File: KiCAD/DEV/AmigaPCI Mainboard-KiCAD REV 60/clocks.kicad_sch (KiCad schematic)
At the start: 46 parts, among them U108 74AHC04, U210 AT27C4096, U211 AT27C4096, U219 74AHCT04, U230 74LVC157, U812 74LVC245, U813 74LVC245, U814 74LVC245, U815 74LVC08, U816 74LVC245, U817 74LVC245, U818 74LVC245, U819 74LVC245, X1 6MHz, X2 33MHz, X3 28.63636MHz

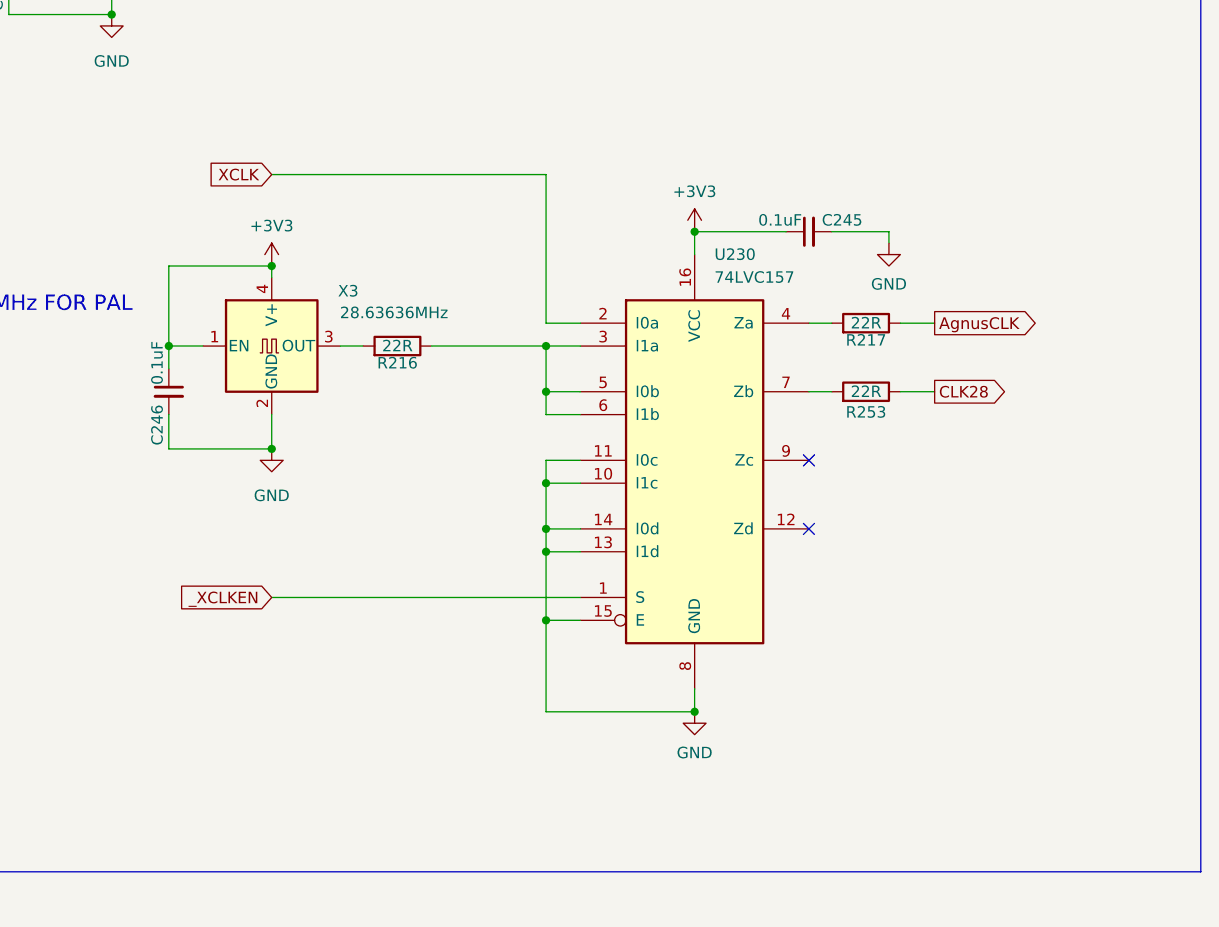
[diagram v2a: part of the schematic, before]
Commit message: APCI Rev 6.0 Work
Eliminate U230 (74LVC147) by moving the clock switching function to U409.
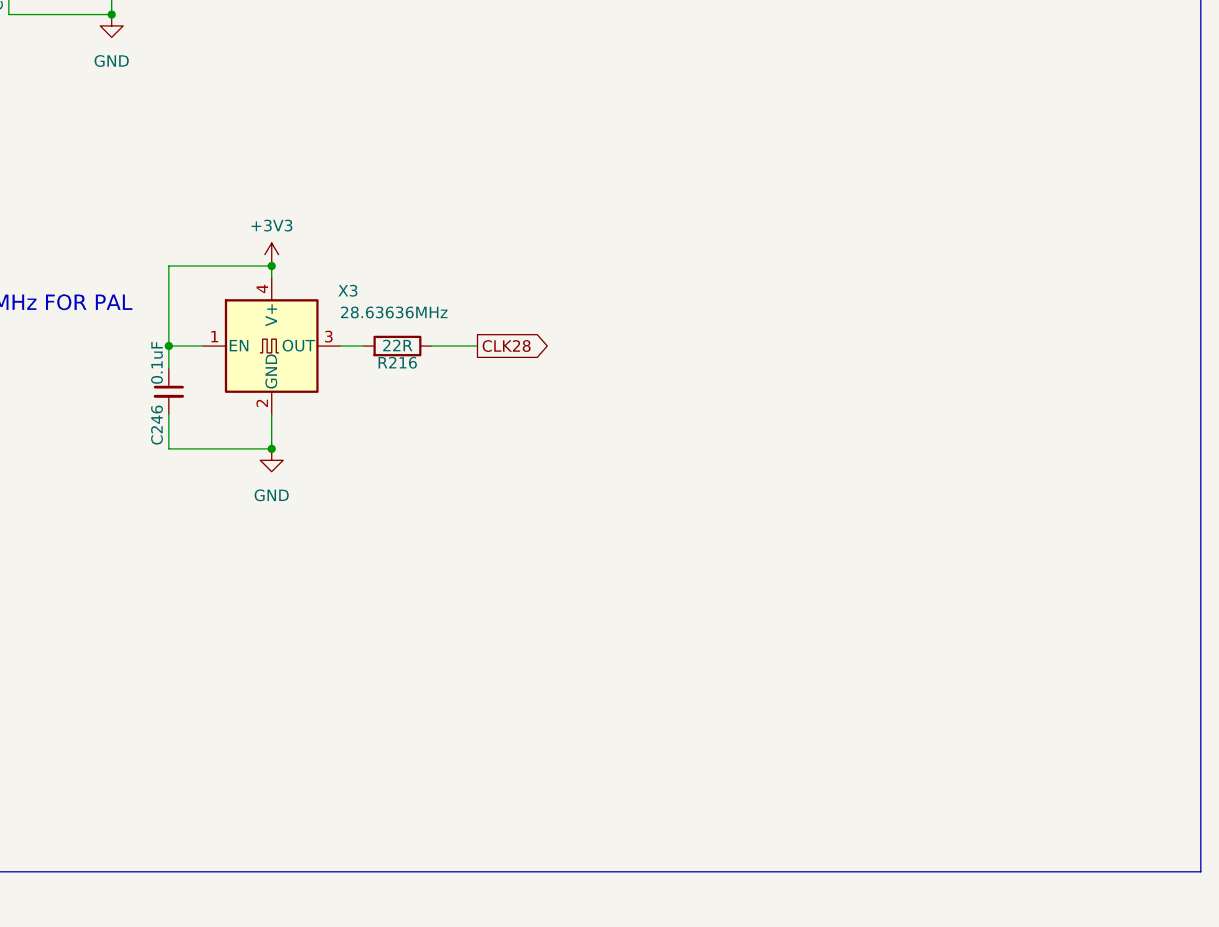
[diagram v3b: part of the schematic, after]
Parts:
- removed C245: 0.1uF, Capacitor_SMD:C_0603_1608Metric, symbol Device:C_Small
- removed R217, R253: 22R, Resistor_SMD:R_0603_1608Metric, symbol Device:R
- removed U230: 74LVC157, Package_SO:TSSOP-16_4.4x5mm_P0.65mm, symbol 74xx:74LS157
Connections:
- net CLK28: now also R216.1
- no-connect marks 2 -> 0

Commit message: Add flash and remove HID buffer.
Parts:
- added C253: 0.1uF, Capacitor_SMD:C_0603_1608Metric, symbol Device:C_Small
- added U223: SST39VF1601C, Package_SO:TSOP-I-48_18.4x12mm_P0.5mm, symbol AmigaPCI-Symbols:SST39VF1601C
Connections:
- net +3V3: now also C253.1, U223.14 (_WP), U223.37 (VDD)
- net GND: now also C253.2, U223.27 (GND), U223.46 (GND)
- new net: U223.10 (NC), U223.13 (NC), U223.47 (NC)
- new net FBANK0: U223.16 (A18)
- new net FBANK1: U223.9 (A19)
- new net FRDY: U223.15 (RY_BY)
- new net LVA1: U223.25 (A0)
- new net LVA10: U223.7 (A9)
- new net LVA11: U223.6 (A10)
- new net LVA12: U223.5 (A11)
- new net LVA13: U223.4 (A12)
- new net LVA14: U223.3 (A13)
- new net LVA15: U223.2 (A14)
- new net LVA16: U223.1 (A15)
- new net LVA17: U223.48 (A16)
- new net LVA18: U223.17 (A17)
- new net LVA2: U223.24 (A1)
- new net LVA3: U223.23 (A2)
- new net LVA4: U223.22 (A3)
- new net LVA5: U223.21 (A4)
- new net LVA6: U223.20 (A5)
- new net LVA7: U223.19 (A6)
- new net LVA8: U223.18 (A7)
- new net LVA9: U223.8 (A8)
- new net LVD16: U223.29 (D0)
- new net LVD17: U223.31 (D1)
- new net LVD18: U223.33 (D2)
- new net LVD19: U223.35 (D3)
- new net LVD20: U223.38 (D4)
- new net LVD21: U223.40 (D5)
- new net LVD22: U223.42 (D6)
- new net LVD23: U223.44 (D7)
- new net LVD24: U223.30 (D8)
- new net LVD25: U223.32 (D9)
- new net LVD26: U223.34 (D10)
- new net LVD27: U223.36 (D11)
- new net LVD28: U223.39 (D12)
- new net LVD29: U223.41 (D13)
- new net LVD30: U223.43 (D14)
- new net LVD31: U223.45 (D15)
- new net _FEN: U223.26 (_CE)
- new net _FRDEN: U223.28 (_OE)
- new net _FRST: U223.12 (_RST)
- new net _FWREN: U223.11 (_WE)
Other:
- note added: "BOTTOM BOOT 1Mx16 FLASH TREATED AS FOUR 512K ADDRESS SPACES AS DEFINED BY FBANKx."
- note added: "FLASH"
- moved on the sheet: C228, C229, C246, C816, C817, C818, C819, R140, R141, R142, R143, R144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

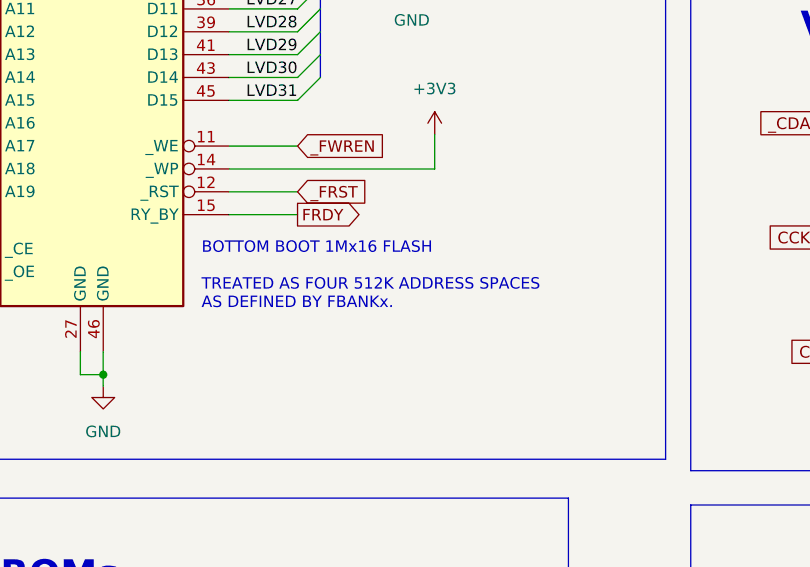
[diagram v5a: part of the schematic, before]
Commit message: APCI Rev 6.0 Work
Added flash and i2c, USB now powered by standbay rail.
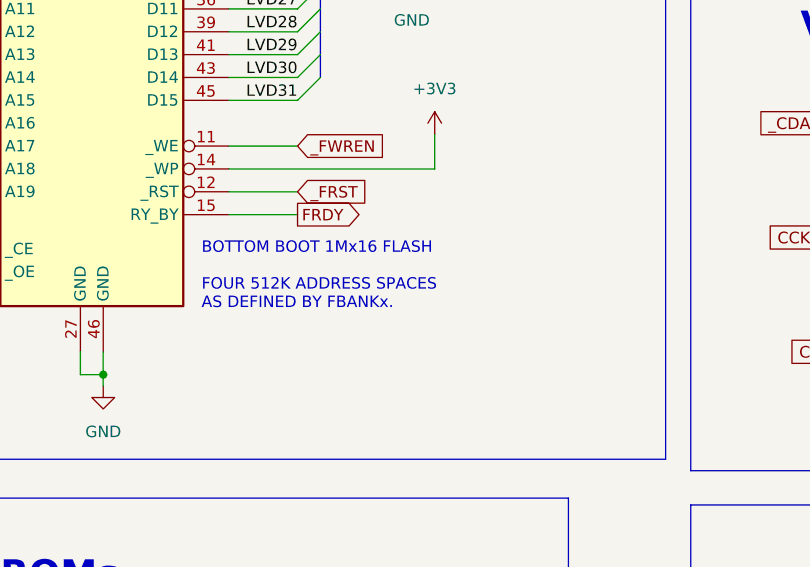
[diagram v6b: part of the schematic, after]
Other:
- note added: "BOTTOM BOOT 1Mx16 FLASH FOUR 512K ADDRESS SPACES AS DEFINED BY FBANKx."
- note removed: "BOTTOM BOOT 1Mx16 FLASH TREATED AS FOUR 512K ADDRESS SPACES AS DEFINED BY FBANKx."
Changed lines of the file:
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@@
 	(title_block
 		(title "AMIGA PCI")
-		(date "2025-06-26")
+		(date "2025-06-27")
 		(rev "6.0")
 	)
@@
 		)
 	)
-	(text "BOTTOM BOOT 1Mx16 FLASH\n\nTREATED AS FOUR 512K ADDRESS SPACES\nAS DEFINED BY FBANKx."
+	(text "BOTTOM BOOT 1Mx16 FLASH\n\nFOUR 512K ADDRESS SPACES\nAS DEFINED BY FBANKx."
 		(exclude_from_sim no)
 		(at 90.932 98.298 0)

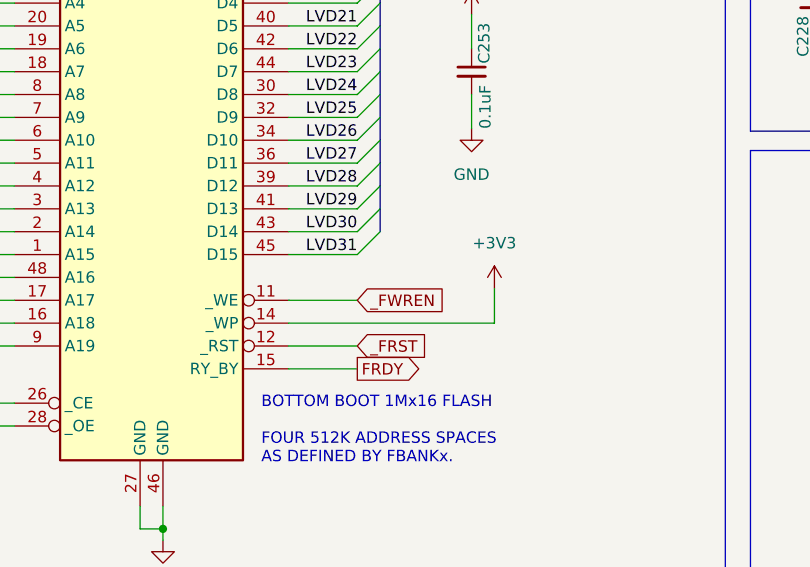
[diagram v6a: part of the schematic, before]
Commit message: APCI Rev 6.0 Work
Add pullups to i2c lines.
Connect Flash _WP to U409.
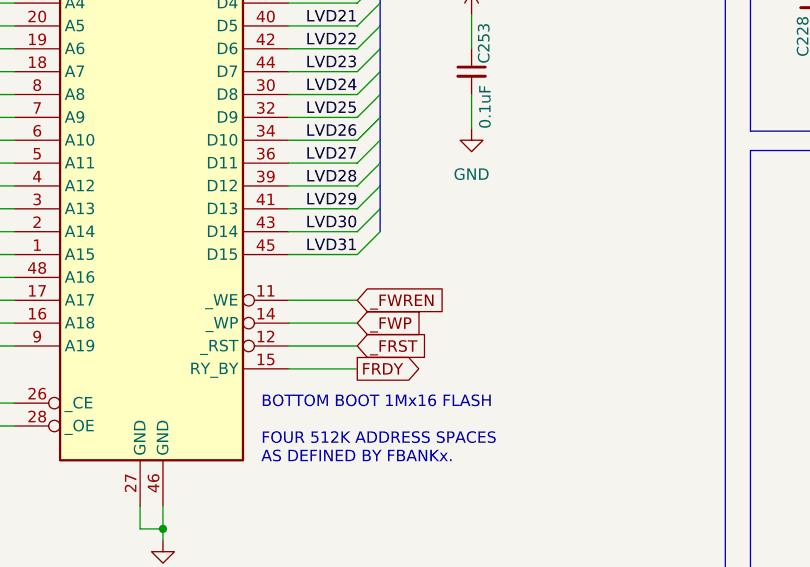
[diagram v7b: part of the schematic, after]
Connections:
- net +3V3: no longer U223.14 (_WP)
- new net _FWP: U223.14 (_WP)
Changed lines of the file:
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@@
 		)
 	)
-	(wire
-		(pts
-			(xy 116.84 82.55) (xy 116.84 86.36)
-		)
-		(stroke
-			(width 0)
-			(type default)
-		)
-	)
 	(bus
 		(pts
@@
 	(wire
 		(pts
+			(xy 101.6 86.36) (xy 93.98 86.36)
+		)
+		(stroke
+			(width 0)
+			(type default)
+		)
+	)
+	(wire
+		(pts
 			(xy 317.5 139.7) (xy 323.85 139.7)
 		)
@@
 	(wire
 		(pts
-			(xy 93.98 86.36) (xy 116.84 86.36)
-		)
-		(stroke
-			(width 0)
-			(type default)
-		)
-	)
-	(wire
-		(pts
 			(xy 325.12 44.45) (xy 317.5 44.45)
 		)
@@
 		)
 	)
+	(global_label "_FWP"
+		(shape input)
+		(at 101.6 86.36 0)
+		(fields_autoplaced yes)
+		(effects
+			(font
+				(size 1.27 1.27)
+			)
+			(justify left)
+		)
+		(property "Intersheetrefs" "${INTERSHEET_REFS}"
+			(at 111.8423 86.36 0)
+			(effects
+				(font
+					(size 1.27 1.27)
+				)
+				(justify left)
+			)
+		)
+	)
 	(global_label "_VC1"
 		(shape output)
@@
 					(unit 1)
 				)
-			)
-		)
-	)
-	(symbol
-		(lib_name "+3V3_1")
-		(lib_id "power:+3V3")
-		(at 116.84 82.55 0)
-		(unit 1)
-		(exclude_from_sim no)
-		(in_bom yes)
-		(on_board yes)
-		(dnp no)
-		(fields_autoplaced yes)
-		(property "Reference" "#PWR149"
-			(at 116.84 86.36 0)
-			(effects
-				(font
-					(size 1.27 1.27)
-				)
-				(hide yes)
-			)
-		)
-		(property "Value" "+3V3"
-			(at 116.84 77.47 0)
-			(effects
-				(font
-					(size 1.27 1.27)
-				)
-			)
-		)
-		(property "Footprint" ""
-			(at 116.84 82.55 0)
-			(effects
-				(font
-					(size 1.27 1.27)
-				)
-				(hide yes)
-			)
-		)
-		(property "Datasheet" ""
-			(at 116.84 82.55 0)
-			(effects
-				(font
-					(size 1.27 1.27)
-				)
-				(hide yes)
-			)
-		)
-		(property "Description" "Power symbol creates a global label with name \"+3V3\""
-			(at 116.84 82.55 0)
-			(effects
-				(font
-					(size 1.27 1.27)
-				)
-				(hide yes)
-			)
-		)
-		(pin "1"
-		)
-		(instances
-			(project "AmigaPCI Mainboard"
-				(path "/72453515-27fe-4336-91f3-e3c8054f7767/d671396a-959f-409b-8612-87cb620c51cb"
-					(reference "#PWR149")
-					(unit 1)
-				)
